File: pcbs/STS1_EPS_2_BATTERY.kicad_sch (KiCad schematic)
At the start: 11 parts, among them J3 Battery Pack, Q4 SI7272DP-T1-GE3, U13 TMCS1101A3B-Q1, U4 BQ29209DRBT

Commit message: worked on sts1_eps_1
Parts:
- removed U13: TMCS1101A3B-Q1, Package_SO:SOIC-8_3.9x4.9mm_P1.27mm, symbol STS_Sensor_Current:TMCS1101Q1
- added C22: 1u, Capacitor_SMD:C_0805_2012Metric, symbol Device:C
- added R32: 40k2, Resistor_SMD:R_0805_2012Metric, symbol Device:R
- added R33: 64k, Resistor_SMD:R_0805_2012Metric, symbol Device:R
- added R34: 31k5, Resistor_SMD:R_0805_2012Metric, symbol Device:R
- added U6: TPS2420RSAT, Package_DFN_QFN:VQFN-16-1EP_3x3mm_P0.5mm_EP1.45x1.45mm_ThermalVias, symbol STS_Power_Management:TPS2420RSAT
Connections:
- net BATT: now also U6.10 (VOUT_2), U6.11 (VOUT_3), U6.12 (VOUT)
- net BATT_I: now also R34.1, U6.13 (IMON)
- net BATT_RAW: now also U6.1 (VIN_2), U6.2 (VIN_3), U6.3 (VIN_4), U6.4 (VIN)
- net GND: now also C22.2, R32.2, R33.2, R34.2, U6.14 (~{PG}), U6.15 (~{FLT}), U6.16 (~{EN}), U6.17 (EP), U6.5 (GND), U6.6 (LTCH)
- new net CT: C22.1, U6.9 (CT)
- new net IFLT: R33.1, U6.8 (IFLT)
- new net IMAX: R32.1, U6.7 (IMAX)
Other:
- note added: "Absolute current limit: 5A Fault current: 3,125A (corresponds to 20W @ 6,4V) Fault timer: ~400ms to trigger, 1s to recover"
- note added: "Overcurrent Protection"
- moved on the sheet: C12, C13, C14, J3, Q4A, Q4B, R21, R22, R23, R39, U4

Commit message: Worked on STS1_EPS_2.
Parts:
- renumbered C22 to C23, C14 to C24, C12 to C25, C13 to C26, J3 to J9, Q4 to Q23, R39 to R38, R34 to R39, R33 to R40, R32 to R41, R21 to R42, R22 to R43, R23 to R44, U4 to U7
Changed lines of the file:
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@@
   (symbol (lib_id "power:GND") (at 93.345 67.31 90) (mirror x) (unit 1)
     (in_bom yes) (on_board yes) (fields_autoplaced)
-    (property "Reference" "#PWR076" (id 0) (at 99.695 67.31 0)
+    (property "Reference" "#PWR096" (id 0) (at 99.695 67.31 0)
       (effects (font (size 1.27 1.27)) hide)
     )
@@
   (symbol (lib_id "STS_Battery_Management:BQ29209DRBT") (at 159.385 69.85 0) (unit 1)
     (in_bom yes) (on_board yes) (fields_autoplaced)
-    (property "Reference" "U4" (id 0) (at 159.385 49.53 0))
+    (property "Reference" "U7" (id 0) (at 159.385 49.53 0))
     (property "Value" "BQ29209DRBT" (id 1) (at 159.385 52.07 0))
     (property "Footprint" "STS_Package_VSON:TI_VSON8" (id 2) (at 159.385 69.85 0)
@@
   (symbol (lib_id "power:GND") (at 93.345 54.61 90) (mirror x) (unit 1)
     (in_bom yes) (on_board yes) (fields_autoplaced)
-    (property "Reference" "#PWR074" (id 0) (at 99.695 54.61 0)
+    (property "Reference" "#PWR094" (id 0) (at 99.695 54.61 0)
       (effects (font (size 1.27 1.27)) hide)
     )
@@
   (symbol (lib_id "Device:C") (at 73.025 97.79 0) (mirror y) (unit 1)
     (in_bom yes) (on_board yes) (fields_autoplaced)
-    (property "Reference" "C22" (id 0) (at 69.215 96.5199 0)
+    (property "Reference" "C23" (id 0) (at 69.215 96.5199 0)
       (effects (font (size 1.27 1.27)) (justify left))
     )
@@
   (symbol (lib_id "power:GND") (at 90.805 105.41 0) (mirror y) (unit 1)
     (in_bom yes) (on_board yes) (fields_autoplaced)
-    (property "Reference" "#PWR078" (id 0) (at 90.805 111.76 0)
+    (property "Reference" "#PWR093" (id 0) (at 90.805 111.76 0)
       (effects (font (size 1.27 1.27)) hide)
     )
@@
   (symbol (lib_id "Device:R") (at 35.56 163.83 0) (unit 1)
     (in_bom yes) (on_board yes) (fields_autoplaced)
-    (property "Reference" "R39" (id 0) (at 41.91 163.83 90))
+    (property "Reference" "R38" (id 0) (at 41.91 163.83 90))
     (property "Value" "1M" (id 1) (at 39.37 163.83 90))
     (property "Footprint" "Resistor_SMD:R_0805_2012Metric" (id 2) (at 33.782 163.83 90)
@@
   (symbol (lib_id "Device:R") (at 90.805 97.79 0) (mirror y) (unit 1)
     (in_bom yes) (on_board yes) (fields_autoplaced)
-    (property "Reference" "R32" (id 0) (at 88.265 96.5199 0)
+    (property "Reference" "R41" (id 0) (at 88.265 96.5199 0)
       (effects (font (size 1.27 1.27)) (justify left))
     )
@@
   (symbol (lib_id "Device:R") (at 62.865 97.79 0) (mirror y) (unit 1)
     (in_bom yes) (on_board yes) (fields_autoplaced)
-    (property "Reference" "R34" (id 0) (at 60.325 96.5199 0)
+    (property "Reference" "R39" (id 0) (at 60.325 96.5199 0)
       (effects (font (size 1.27 1.27)) (justify left))
     )
@@
   (symbol (lib_id "power:GND") (at 73.025 105.41 0) (mirror y) (unit 1)
     (in_bom yes) (on_board yes) (fields_autoplaced)
-    (property "Reference" "#PWR080" (id 0) (at 73.025 111.76 0)
+    (property "Reference" "#PWR091" (id 0) (at 73.025 111.76 0)
       (effects (font (size 1.27 1.27)) hide)
     )
@@
   (symbol (lib_id "power:GNDREF") (at 135.255 88.9 0) (unit 1)
     (in_bom yes) (on_board yes) (fields_autoplaced)
-    (property "Reference" "#PWR0109" (id 0) (at 135.255 95.25 0)
+    (property "Reference" "#PWR098" (id 0) (at 135.255 95.25 0)
       (effects (font (size 1.27 1.27)) hide)
     )
@@
   (symbol (lib_id "Device:C_Polarized") (at 135.255 82.55 0) (unit 1)
     (in_bom yes) (on_board yes) (fields_autoplaced)
-    (property "Reference" "C14" (id 0) (at 139.065 81.2799 0)
+    (property "Reference" "C24" (id 0) (at 139.065 81.2799 0)
       (effects (font (size 1.27 1.27)) (justify left))
     )
@@
   (symbol (lib_id "power:GND") (at 93.345 62.23 90) (mirror x) (unit 1)
     (in_bom yes) (on_board yes) (fields_autoplaced)
-    (property "Reference" "#PWR075" (id 0) (at 99.695 62.23 0)
+    (property "Reference" "#PWR095" (id 0) (at 99.695 62.23 0)
       (effects (font (size 1.27 1.27)) hide)
     )
@@
   (symbol (lib_id "Connector_Generic:Conn_01x04") (at 198.12 41.91 0) (unit 1)
     (in_bom yes) (on_board yes)
-    (property "Reference" "J3" (id 0) (at 197.485 34.29 0))
+    (property "Reference" "J9" (id 0) (at 197.485 34.29 0))
     (property "Value" "Battery Pack" (id 1) (at 199.39 36.83 0))
     (property "Footprint" "STS_Connector:436500415" (id 2) (at 198.12 41.91 0)
@@
   (symbol (lib_id "power:GNDREF") (at 178.435 88.9 0) (unit 1)
     (in_bom yes) (on_board yes) (fields_autoplaced)
-    (property "Reference" "#PWR0108" (id 0) (at 178.435 95.25 0)
+    (property "Reference" "#PWR0100" (id 0) (at 178.435 95.25 0)
       (effects (font (size 1.27 1.27)) hide)
     )
@@
   (symbol (lib_id "STS_Transistor_FET:SI7272DP-T1-GE3") (at 53.975 170.815 0) (mirror x) (unit 1)
     (in_bom yes) (on_board yes)
-    (property "Reference" "Q4" (id 0) (at 68.58 179.07 0))
+    (property "Reference" "Q23" (id 0) (at 68.58 179.07 0))
     (property "Value" "SI7272DP-T1-GE3" (id 1) (at 76.2 181.61 0))
     (property "Footprint" "STS_Package_SO:POWERPAK_SO8" (id 2) (at 59.817 169.545 0)
@@
   (symbol (lib_id "Device:R") (at 150.495 123.825 180) (unit 1)
     (in_bom yes) (on_board yes) (fields_autoplaced)
-    (property "Reference" "R21" (id 0) (at 153.035 122.5549 0)
+    (property "Reference" "R42" (id 0) (at 153.035 122.5549 0)
       (effects (font (size 1.27 1.27)) (justify right))
     )
@@
   (symbol (lib_id "STS_Transistor_FET:SI7272DP-T1-GE3") (at 41.275 170.815 0) (mirror x) (unit 2)
     (in_bom yes) (on_board yes)
-    (property "Reference" "Q4" (id 0) (at 38.735 178.435 0))
+    (property "Reference" "Q23" (id 0) (at 38.735 178.435 0))
     (property "Value" "SI7272DP-T1-GE3" (id 1) (at 31.75 180.975 0))
     (property "Footprint" "STS_Package_SO:POWERPAK_SO8" (id 2) (at 47.117 169.545 0)
@@
   (symbol (lib_id "Device:C") (at 161.925 121.285 0) (unit 1)
     (in_bom yes) (on_board yes) (fields_autoplaced)
-    (property "Reference" "C13" (id 0) (at 165.735 120.0149 0)
+    (property "Reference" "C26" (id 0) (at 165.735 120.0149 0)
       (effects (font (size 1.27 1.27)) (justify left))
     )
@@
   (symbol (lib_id "power:GND") (at 57.785 57.15 270) (mirror x) (unit 1)
     (in_bom yes) (on_board yes) (fields_autoplaced)
-    (property "Reference" "#PWR091" (id 0) (at 51.435 57.15 0)
+    (property "Reference" "#PWR088" (id 0) (at 51.435 57.15 0)
       (effects (font (size 1.27 1.27)) hide)
     )
@@
   (symbol (lib_id "Device:R") (at 155.575 106.045 90) (unit 1)
     (in_bom yes) (on_board yes) (fields_autoplaced)
-    (property "Reference" "R22" (id 0) (at 155.575 99.695 90))
+    (property "Reference" "R43" (id 0) (at 155.575 99.695 90))
     (property "Value" "140" (id 1) (at 155.575 102.235 90))
     (property "Footprint" "Resistor_SMD:R_0805_2012Metric" (id 2) (at 155.575 107.823 90)
@@
   (symbol (lib_id "Device:C") (at 161.925 109.855 0) (unit 1)
     (in_bom yes) (on_board yes) (fields_autoplaced)
-    (property "Reference" "C12" (id 0) (at 165.735 108.5849 0)
+    (property "Reference" "C25" (id 0) (at 165.735 108.5849 0)
       (effects (font (size 1.27 1.27)) (justify left))
     )
@@
   (symbol (lib_id "power:GND") (at 55.245 184.15 0) (unit 1)
     (in_bom yes) (on_board yes) (fields_autoplaced)
-    (property "Reference" "#PWR0106" (id 0) (at 55.245 190.5 0)
+    (property "Reference" "#PWR087" (id 0) (at 55.245 190.5 0)
       (effects (font (size 1.27 1.27)) hide)
     )
@@
   (symbol (lib_id "power:GND") (at 81.915 105.41 0) (mirror y) (unit 1)
     (in_bom yes) (on_board yes) (fields_autoplaced)
-    (property "Reference" "#PWR079" (id 0) (at 81.915 111.76 0)
+    (property "Reference" "#PWR092" (id 0) (at 81.915 111.76 0)
       (effects (font (size 1.27 1.27)) hide)
     )
@@
   (symbol (lib_id "Device:R") (at 81.915 97.79 0) (mirror y) (unit 1)
     (in_bom yes) (on_board yes) (fields_autoplaced)
-    (property "Reference" "R33" (id 0) (at 79.375 96.5199 0)
+    (property "Reference" "R40" (id 0) (at 79.375 96.5199 0)
       (effects (font (size 1.27 1.27)) (justify left))
     )
@@
   (symbol (lib_id "power:GNDREF") (at 161.925 130.175 0) (unit 1)
     (in_bom yes) (on_board yes) (fields_autoplaced)
-    (property "Reference" "#PWR0107" (id 0) (at 161.925 136.525 0)
+    (property "Reference" "#PWR099" (id 0) (at 161.925 136.525 0)
       (effects (font (size 1.27 1.27)) hide)
     )
@@
   (symbol (lib_id "Device:R") (at 155.575 116.205 90) (unit 1)
     (in_bom yes) (on_board yes) (fields_autoplaced)
-    (property "Reference" "R23" (id 0) (at 155.575 109.855 90))
+    (property "Reference" "R44" (id 0) (at 155.575 109.855 90))
     (property "Value" "140" (id 1) (at 155.575 112.395 90))
     (property "Footprint" "Resistor_SMD:R_0805_2012Metric" (id 2) (at 155.575 117.983 90)
@@
   (symbol (lib_id "power:GND") (at 57.785 59.69 270) (mirror x) (unit 1)
     (in_bom yes) (on_board yes) (fields_autoplaced)
-    (property "Reference" "#PWR092" (id 0) (at 51.435 59.69 0)
+    (property "Reference" "#PWR089" (id 0) (at 51.435 59.69 0)
       (effects (font (size 1.27 1.27)) hide)
     )
@@
   (symbol (lib_id "power:GND") (at 93.345 72.39 90) (mirror x) (unit 1)
     (in_bom yes) (on_board yes) (fields_autoplaced)
-    (property "Reference" "#PWR077" (id 0) (at 99.695 72.39 0)
-      (effects (font (size 1.27 1.27)) hide)
-    )
+    (property "Reference" "#PWR097" (id 0) (at 99.695 72.39 0)
+      (effects (font (size 1.27 1.27)) hide)
+    )

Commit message: Worked on STS1_EPS_2.
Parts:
- added R4: 0, Resistor_SMD:R_0805_2012Metric, symbol Device:R
- added R45: 64k, Resistor_SMD:R_0805_2012Metric, symbol Device:R
- added TP14: TestPoint, TestPoint:TestPoint_THTPad_D1.0mm_Drill0.5mm, symbol Connector:TestPoint
- added U9: 4072, Package_SO:SOIC-14_3.9x8.7mm_P1.27mm, symbol 4xxx:4072
- J9: footprint STS_Connector:436500415 -> STS_Connector:MOLEX_2078430004; Part (none) -> MOLEX KK Plus 250 Header
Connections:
- net GND: now also R4.2, U9.10, U9.11, U9.12, U9.7 (VSS), U9.9
- net GNDREF: now also R4.1
- net NTC: now also R45.1; no longer J9.4 (Pin_4)
- net DS4_SIGNAL_1: no longer names the net of Q23.2 (G1), Q23.4 (G2), R38.2
- net DS4_SIGNAL_1: now also TP14.1, U9.1
- new net: J9.4 (Pin_4), R45.2
- new net +5V: U9.14 (VDD)
- new net DS1_SIGNAL: U9.4
- new net DS2_SIGNAL: U9.5
- new net RBF_SIGNAL: U9.2
- new net UVLO_SIGNAL: U9.3
- no-connect marks 1 -> 2
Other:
- note added: "Deployment Switch (DS1 + DS2 + RBF) + UVLO"
- note removed: "Deployment Switch (DS4)"
- moved on the sheet: Q23A, Q23B, R38

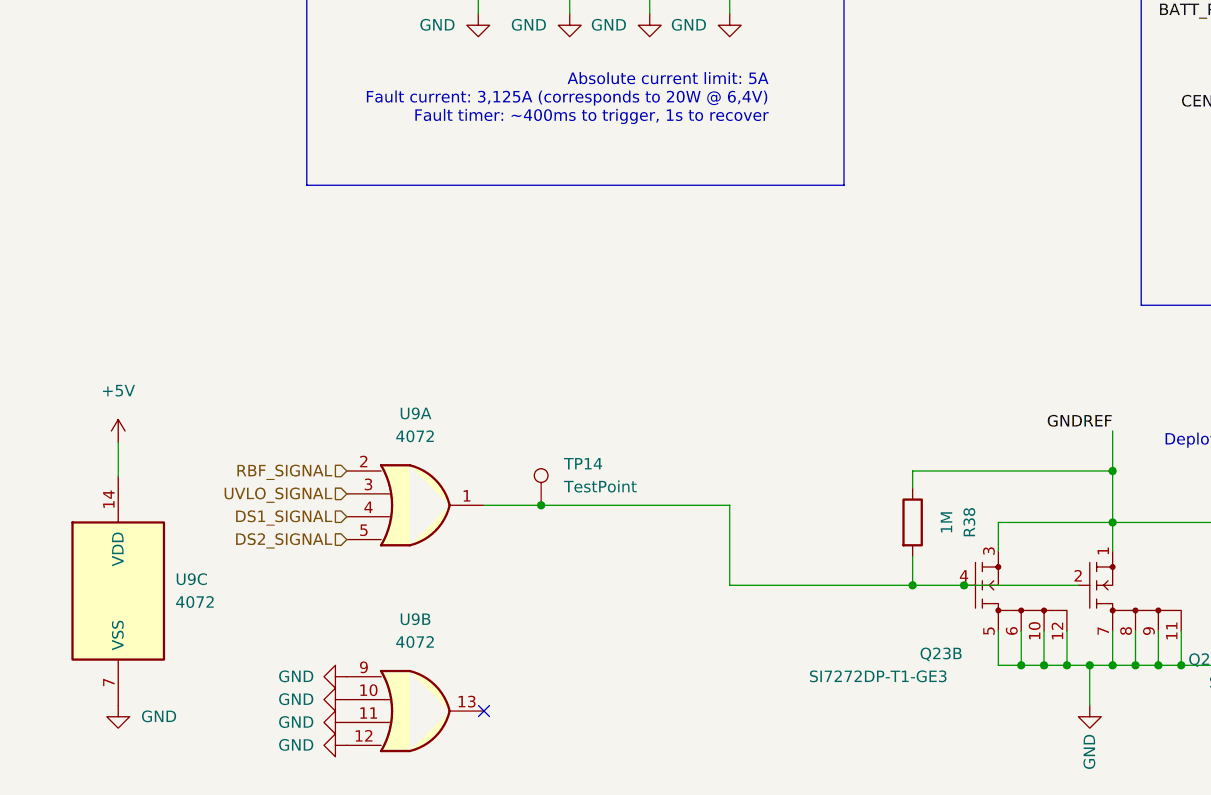
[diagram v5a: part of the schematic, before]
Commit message: Added a logic voltage, so that the deployment circuit breaker FETs also work, when battery is fails.
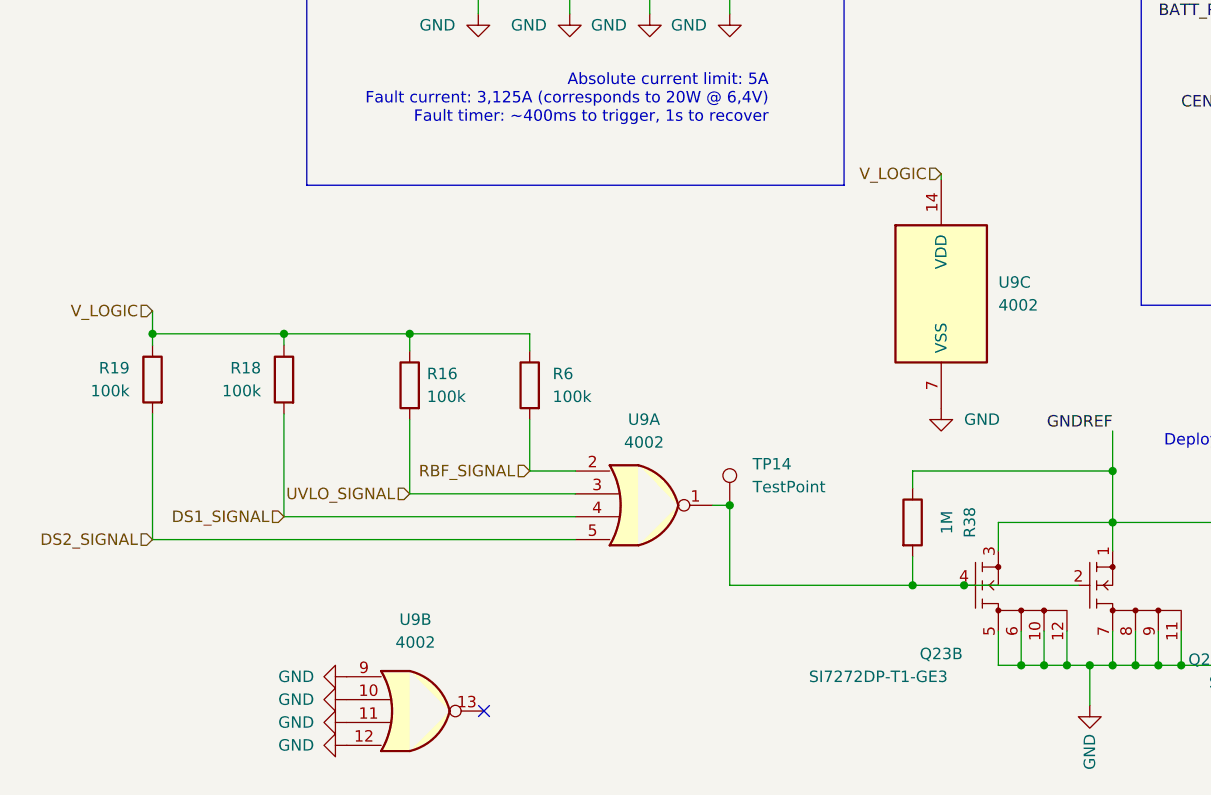
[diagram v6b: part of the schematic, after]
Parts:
- removed U9: 4072, Package_SO:SOIC-14_3.9x8.7mm_P1.27mm, symbol 4xxx:4072
- added R16, R18, R19, R6: 100k, Resistor_SMD:R_0805_2012Metric, symbol Device:R
- added U9: 4002, Package_SO:SOIC-14_3.9x8.7mm_P1.27mm, symbol 4xxx:4002
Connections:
- net DS1_SIGNAL: now also R18.2, U9.4
- net DS2_SIGNAL: now also R19.2, U9.5
- net GND: now also U9.10, U9.11, U9.12, U9.7 (VSS), U9.9
- net RBF_SIGNAL: now also R6.2, U9.2
- net UVLO_SIGNAL: now also R16.2, U9.3
- net at Q23.2 (G1), Q23.4 (G2), R38.2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: now also U9.1
- new net V_LOGIC: R16.1, R18.1, R19.1, R6.1, U9.14 (VDD)
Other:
- moved on the sheet: TP14
